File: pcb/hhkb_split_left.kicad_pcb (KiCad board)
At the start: 2 copper layers, 140.4 x 97.4 mm, 74 parts, among them SW1 Esc, SW10 E, SW11 R, SW12 T, SW13 Ctrl, SW14 A, SW15 S, SW16 D, SW17 F, SW18 G, SW19 Shift, SW2 1, SW20 Z, SW21 X, SW22 C, SW23 V, SW24 B, SW25 Alt, SW26 Meta, SW27 L-Space, SW3 2, SW4 3, SW5 4, SW6 5, SW7 Tab, SW8 Q, SW9 W, U1 74LVC595

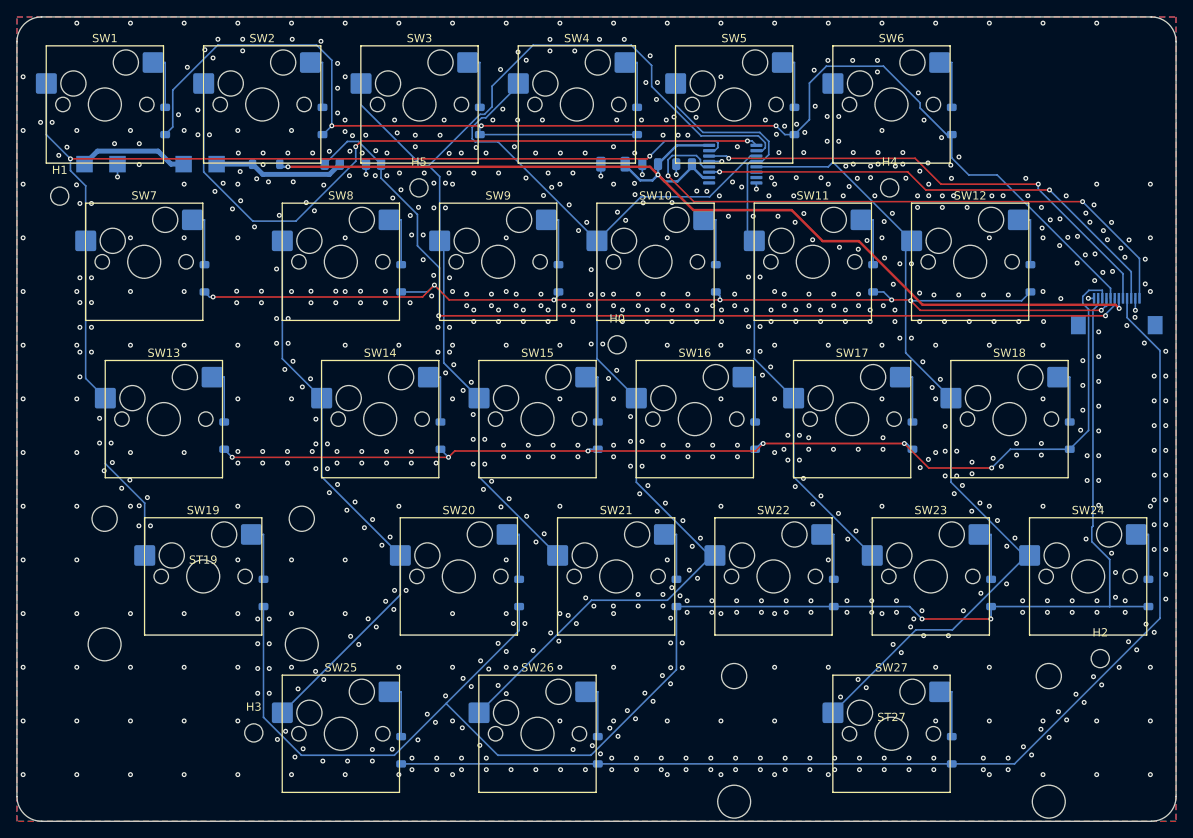
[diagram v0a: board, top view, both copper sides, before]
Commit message: 右基板 COL8/V3V3 の未配線を中継ビアで解消した
Freerouting が SW17-SW31 間（COL8）を毎回配線し損ねていた。
部分配線を見ると、SW17 から南（SW31 方向）への探索を一度も
試みず、北の混雑領域へ迷い込んで力尽きていた——基板の物理的な
制約ではなく、探索ヒューリスティックが局所解にはまったもの。

2点間の中間に同じネットのビアを1個置き、Freeroutingにとって
「近距離問題2つ」に分割することで解決（実測5回連続成功）。

副作用があった。COL8側にビアを足すと、無関係なはずのV3V3
（D_PWR→J_DB、パッド幅0.30mmで元々ギリギリ）が5回連続で
未配線になった。Freerouting内部の配線順序が変わり、際どい
ネットにしわ寄せが行っただけと判断し、V3V3側にも中継ビアを
足して両立させた（2回連続成功で確認）。

右基板専用（左基板ではこの詰まりが起きていない）。

確認: DRC 左右とも違反0・未配線0（実測、ハッシュ一致）。
pytest tools/test_pcb.py -k drc 6件全通過。
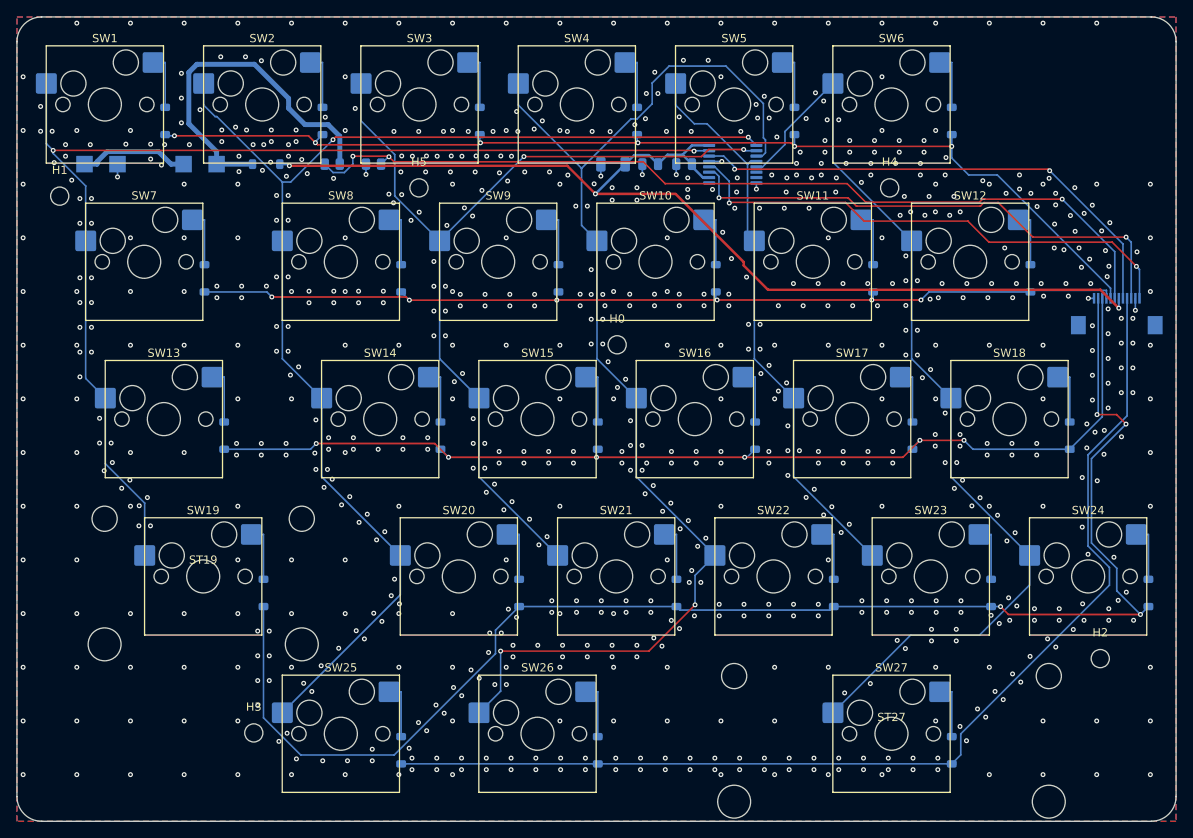
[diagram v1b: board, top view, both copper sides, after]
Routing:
- net ROW0: track 172.9 -> 130.7 mm, vias 3 -> 6
- net VBATT_SW: track 15.9 -> 43.2 mm
- net ROW1: track 136.8 -> 115.6 mm, vias 7 -> 6
- net ROW3: track 195.6 -> 178.1 mm, vias 2 -> 4
- net COL2: track 124.0 -> 110.0 mm, vias 0 -> 2
- net COL3: track 133.5 -> 146.2 mm, vias 0 -> 2
- net CS: track 74.1 -> 62.4 mm
- net COL5: track 108.7 -> 115.2 mm
- net ROW4: track 139.6 -> 134.0 mm
- net COL4: track 74.0 -> 69.1 mm
- net COL1: track 156.8 -> 152.2 mm
- net VBATT_SENSE: track 113.8 -> 109.6 mm, vias 2 -> 3
- net ROW2: track 134.2 -> 130.1 mm
- net SPI_SCK: track 59.4 -> 63.3 mm
- net SPI_MOSI: track 59.3 -> 61.3 mm
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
